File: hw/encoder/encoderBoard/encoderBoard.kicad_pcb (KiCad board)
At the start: 2 copper layers, 20 x 10 mm, 6 parts, among them J1 Conn_01x03, U1 MH253

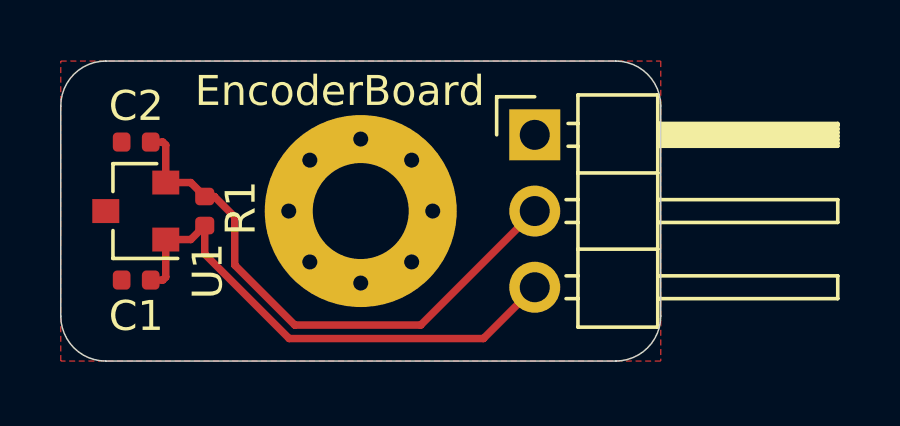
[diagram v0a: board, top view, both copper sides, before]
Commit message: Swap pinhead pinout, add GND polygon to bottom
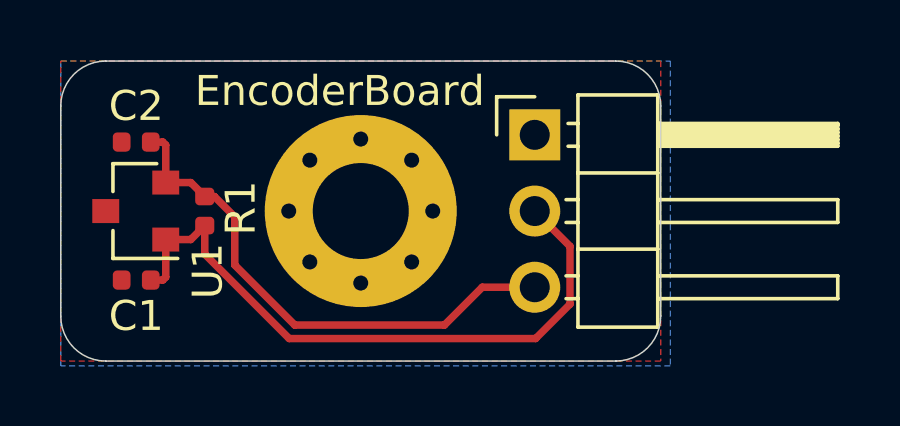
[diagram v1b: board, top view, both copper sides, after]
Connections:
- J1 pad 2: Net-(C2-Pad1) -> VCC
- J1 pad 3: VCC -> Net-(C2-Pad1)
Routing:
- net VCC: track 17.1 -> 21.6 mm
- net Net-(C2-Pad1): track 18.6 -> 17.5 mm
- added copper zone on B.Cu, net GND
